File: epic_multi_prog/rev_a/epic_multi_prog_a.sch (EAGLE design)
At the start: 25 parts, among them J1 EPIC-PROG-PORT, J2 MICRO_USB_B_HIROSE_ZX62R-B-5P, J3 MEC1-105-02-XX-XX-D-A, J4 TAG_CONNECT_HEADER_EPIC, U1 FT232RL, U2 MAX1555

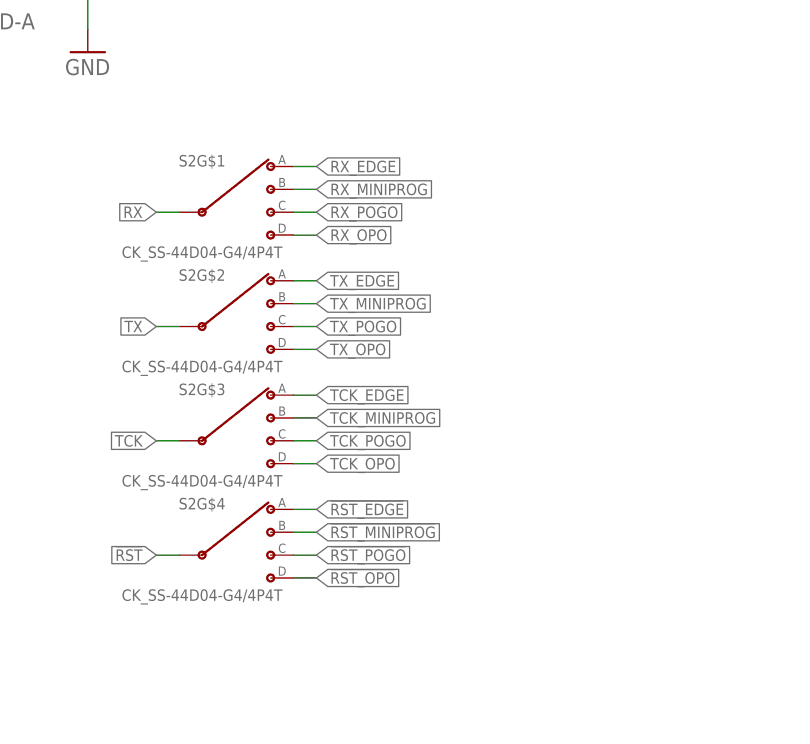
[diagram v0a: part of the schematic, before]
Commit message: Test routing to see how this board is going to look
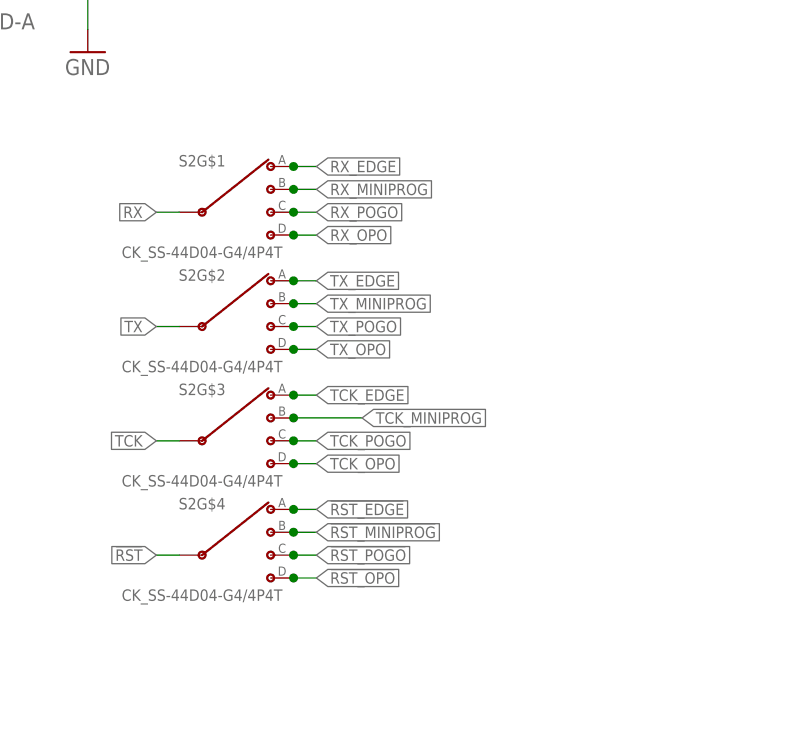
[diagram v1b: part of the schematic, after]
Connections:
- new net !RST_OPO: S2G$4.D
- new net RX_OPO: S2G$1.D
- new net TCK_OPO: S2G$3.D
- new net TX_OPO: S2G$2.D
- net !RST_EDGE: now also S2G$4.A
- net !RST_MINIPROG: now also S2G$4.B
- net !RST_POGO: now also S2G$4.C
- net TCK_EDGE: now also S2G$3.A
- net TCK_MINIPROG: now also S2G$3.B
- net TCK_POGO: now also S2G$3.C
- net TX_EDGE: now also S2G$2.A
- net TX_MINIPROG: now also S2G$2.B
- net TX_POGO: now also S2G$2.C
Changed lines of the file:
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@@
 <wire x1="190.5" y1="96.52" x2="193.04" y2="96.52" width="0.1524" layer="91"/>
 <label x="193.04" y="96.52" size="1.27" layer="95" xref="yes"/>
+<pinref part="S2" gate="G$2" pin="A"/>
+<junction x="190.5" y="96.52"/>
 </segment>
 <segment>
@@
 <wire x1="190.5" y1="93.98" x2="193.04" y2="93.98" width="0.1524" layer="91"/>
 <label x="193.04" y="93.98" size="1.27" layer="95" xref="yes"/>
+<pinref part="S2" gate="G$2" pin="B"/>
+<junction x="190.5" y="93.98"/>
 </segment>
 </net>
@@
 <wire x1="190.5" y1="91.44" x2="193.04" y2="91.44" width="0.1524" layer="91"/>
 <label x="193.04" y="91.44" size="1.27" layer="95" xref="yes"/>
+<pinref part="S2" gate="G$2" pin="C"/>
+<junction x="190.5" y="91.44"/>
 </segment>
 <segment>
@@
 <wire x1="190.5" y1="88.9" x2="193.04" y2="88.9" width="0.1524" layer="91"/>
 <label x="193.04" y="88.9" size="1.27" layer="95" xref="yes"/>
+<pinref part="S2" gate="G$2" pin="D"/>
+<junction x="190.5" y="88.9"/>
 </segment>
 </net>
@@
 <wire x1="190.5" y1="101.6" x2="193.04" y2="101.6" width="0.1524" layer="91"/>
 <label x="193.04" y="101.6" size="1.27" layer="95" xref="yes"/>
+<pinref part="S2" gate="G$1" pin="D"/>
+<junction x="190.5" y="101.6"/>
 </segment>
 </net>
@@
 <wire x1="190.5" y1="104.14" x2="193.04" y2="104.14" width="0.1524" layer="91"/>
 <label x="193.04" y="104.14" size="1.27" layer="95" xref="yes"/>
+<junction x="190.5" y="104.14"/>
 </segment>
 <segment>
@@
 <wire x1="193.04" y1="106.68" x2="190.5" y2="106.68" width="0.1524" layer="91"/>
 <label x="193.04" y="106.68" size="1.27" layer="95" xref="yes"/>
+<junction x="190.5" y="106.68"/>
 </segment>
 </net>
@@
 <wire x1="190.5" y1="109.22" x2="193.04" y2="109.22" width="0.1524" layer="91"/>
 <label x="193.04" y="109.22" size="1.27" layer="95" xref="yes"/>
+<junction x="190.5" y="109.22"/>
 </segment>
 <segment>
@@
 <wire x1="190.5" y1="63.5" x2="193.04" y2="63.5" width="0.1524" layer="91"/>
 <label x="193.04" y="63.5" size="1.27" layer="95" xref="yes"/>
+<pinref part="S2" gate="G$4" pin="D"/>
+<junction x="190.5" y="63.5"/>
 </segment>
 </net>
 <net name="TCK_EDGE" class="0">
-<segment>
-<wire x1="190.5" y1="83.82" x2="193.04" y2="83.82" width="0.1524" layer="91"/>
-<label x="193.04" y="83.82" size="1.27" layer="95" xref="yes"/>
-</segment>
 <segment>
 <pinref part="J3" gate="G$1" pin="9"/>
@@
 <label x="127" y="129.54" size="1.27" layer="95" rot="R180" xref="yes"/>
 </segment>
+<segment>
+<pinref part="S2" gate="G$3" pin="A"/>
+<wire x1="190.5" y1="83.82" x2="193.04" y2="83.82" width="0.1524" layer="91"/>
+<label x="193.04" y="83.82" size="1.27" layer="95" xref="yes"/>
+<junction x="190.5" y="83.82"/>
+</segment>
 </net>
 <net name="TCK_MINIPROG" class="0">
 <segment>
-<wire x1="190.5" y1="81.28" x2="193.04" y2="81.28" width="0.1524" layer="91"/>
-<label x="193.04" y="81.28" size="1.27" layer="95" xref="yes"/>
+<wire x1="190.5" y1="81.28" x2="198.12" y2="81.28" width="0.1524" layer="91"/>
+<label x="198.12" y="81.28" size="1.27" layer="95" xref="yes"/>
+<pinref part="S2" gate="G$3" pin="B"/>
+<junction x="190.5" y="81.28"/>
 </segment>
 <segment>
@@
 <wire x1="190.5" y1="78.74" x2="193.04" y2="78.74" width="0.1524" layer="91"/>
 <label x="193.04" y="78.74" size="1.27" layer="95" xref="yes"/>
+<pinref part="S2" gate="G$3" pin="C"/>
+<junction x="190.5" y="78.74"/>
 </segment>
 <segment>
@@
 <wire x1="190.5" y1="76.2" x2="193.04" y2="76.2" width="0.1524" layer="91"/>
 <label x="193.04" y="76.2" size="1.27" layer="95" xref="yes"/>
+<pinref part="S2" gate="G$3" pin="D"/>
+<junction x="190.5" y="76.2"/>
 </segment>
 </net>
@@
 <wire x1="190.5" y1="71.12" x2="193.04" y2="71.12" width="0.1524" layer="91"/>
 <label x="193.04" y="71.12" size="1.27" layer="95" xref="yes"/>
+<pinref part="S2" gate="G$4" pin="A"/>
+<junction x="190.5" y="71.12"/>
 </segment>
 <segment>
@@
 <wire x1="190.5" y1="68.58" x2="193.04" y2="68.58" width="0.1524" layer="91"/>
 <label x="193.04" y="68.58" size="1.27" layer="95" xref="yes"/>
+<pinref part="S2" gate="G$4" pin="B"/>
+<junction x="190.5" y="68.58"/>
 </segment>
 <segment>
@@
 <wire x1="190.5" y1="66.04" x2="193.04" y2="66.04" width="0.1524" layer="91"/>
 <label x="193.04" y="66.04" size="1.27" layer="95" xref="yes"/>
-</segment>
-<segment>
+<pinref part="S2" gate="G$4" pin="C"/>
+<junction x="190.5" y="66.04"/>
+</segment>
+<segment>

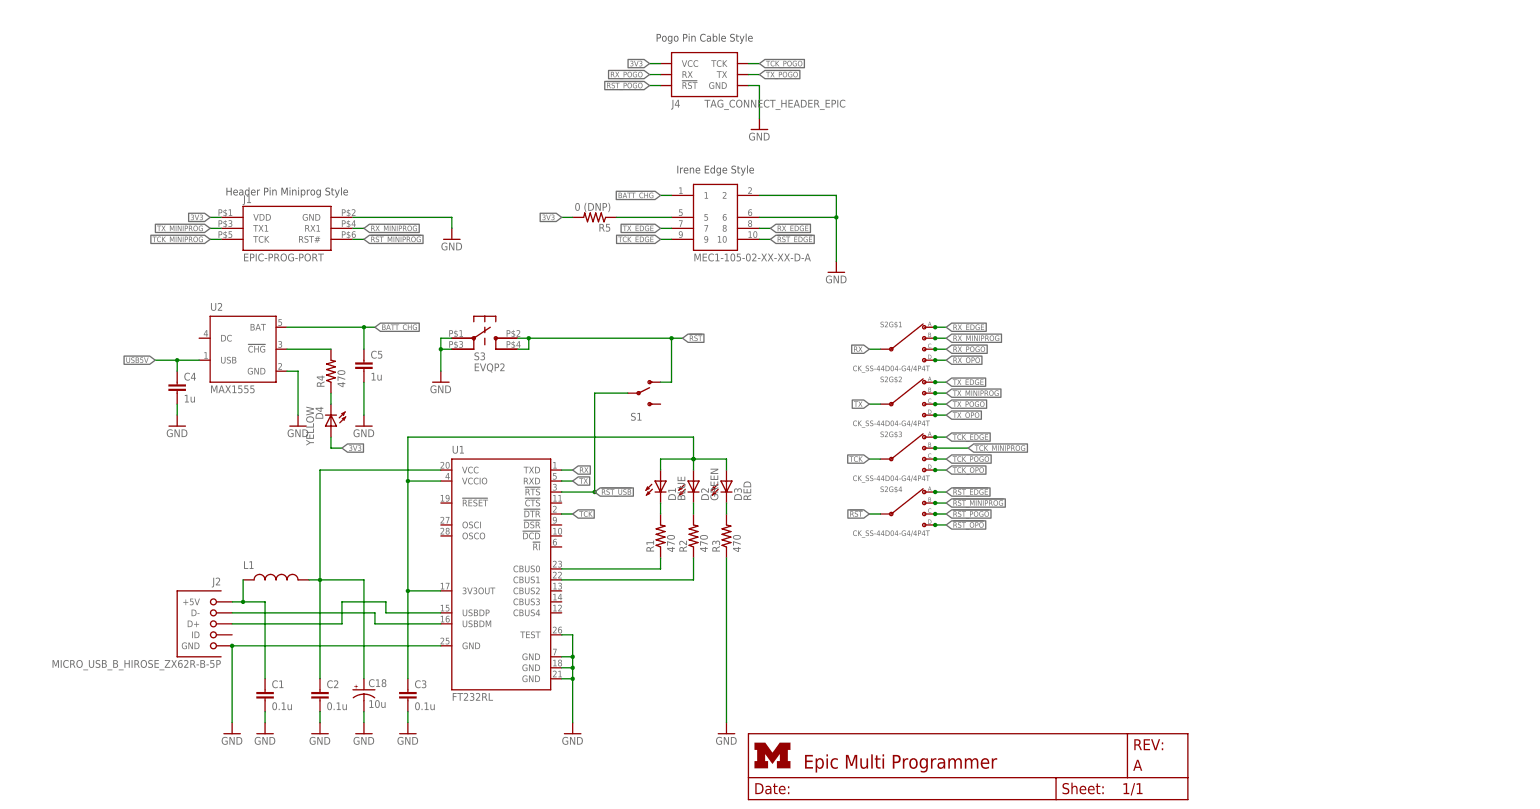
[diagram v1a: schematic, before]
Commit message: added power switches, moving things around
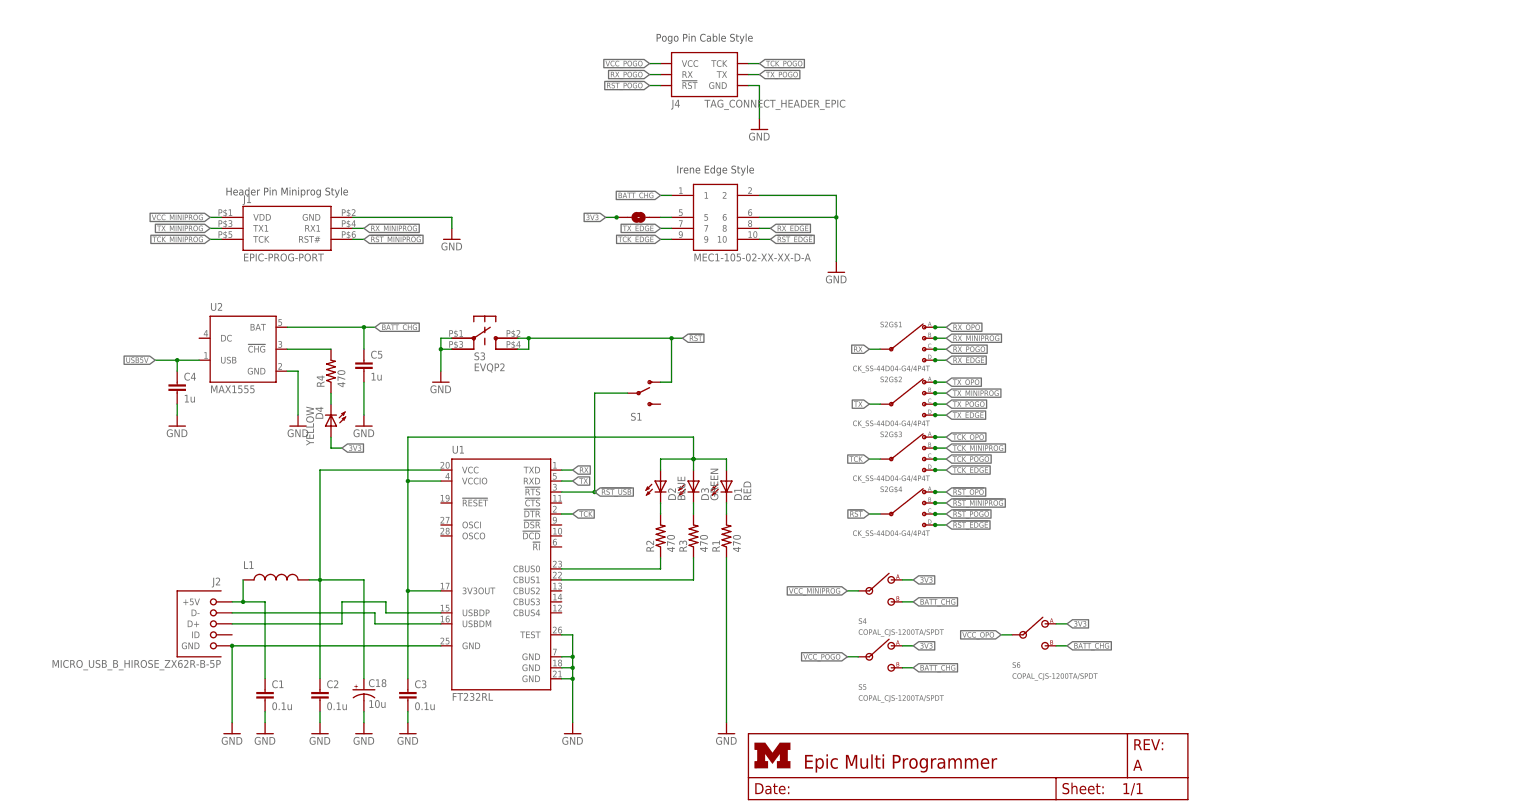
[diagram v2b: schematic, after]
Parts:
- removed R5: 0 (DNP), rcl:R-US_R0603
- added S4, S5, S6: COPAL_CJS-1200TA/SPDT, switches:COPAL_CJS-1200TA/SPDT
- added SJ1: SOLDERJUMPERNO, SparkFun-Passives:SOLDERJUMPERNO
- D1: value BLUE -> RED
- D2: value GREEN -> BLUE
- D3: value RED -> GREEN
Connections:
- new net VCC_MINIPROG: J1.VDD, S4.IN
- new net VCC_OPO: S6.IN
- new net VCC_POGO: J4.VCC, S5.IN
- net !RST_EDGE: now also S2G$4.D; no longer S2G$4.A
- net !RST_OPO: now also S2G$4.A; no longer S2G$4.D
- net 3V3: now also S4.A, S5.A, S6.A, SJ1.1; no longer J1.VDD, J4.VCC, R5.2
- net BATT_CHG: now also S4.B, S5.B, S6.B
- net GND: now also R1.1; no longer R3.1
- net N$1: now also SJ1.2; no longer R5.1
- net N$10: now also R2.1; no longer R1.1
- net N$11: now also R3.1; no longer R2.1
- net RX_EDGE: now also S2G$1.D; no longer S2G$1.A
- net RX_OPO: now also S2G$1.A; no longer S2G$1.D
- net TCK_EDGE: now also S2G$3.D; no longer S2G$3.A
- net TCK_OPO: now also S2G$3.A; no longer S2G$3.D
- net TX_EDGE: now also S2G$2.D; no longer S2G$2.A
- net TX_OPO: now also S2G$2.A; no longer S2G$2.D
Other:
- moved on the sheet: D1, D2, D3, R1, R2, R3

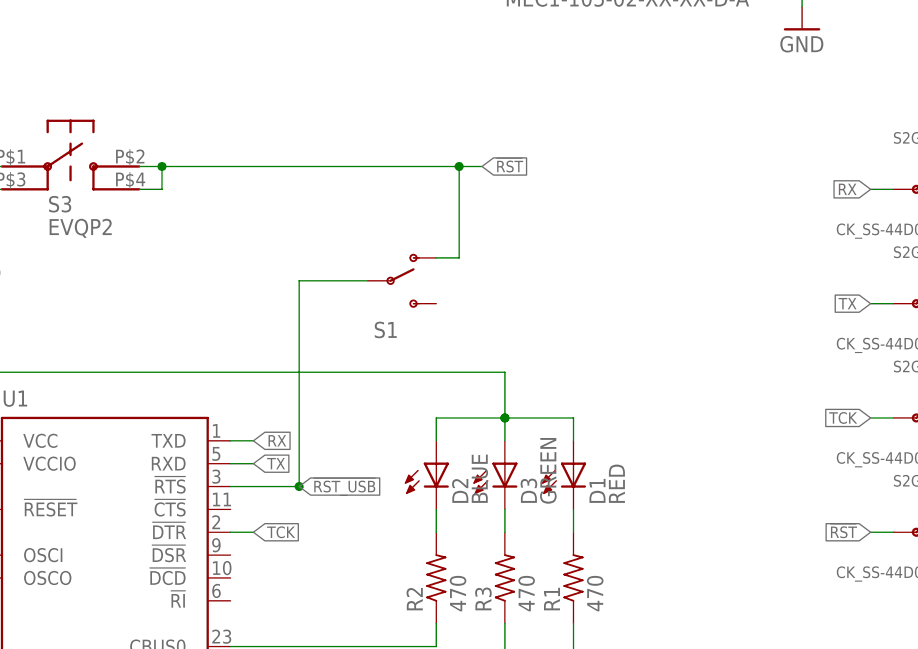
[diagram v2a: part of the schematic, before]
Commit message: Moved uart/prog switch
Planning on the huge smd micro usb
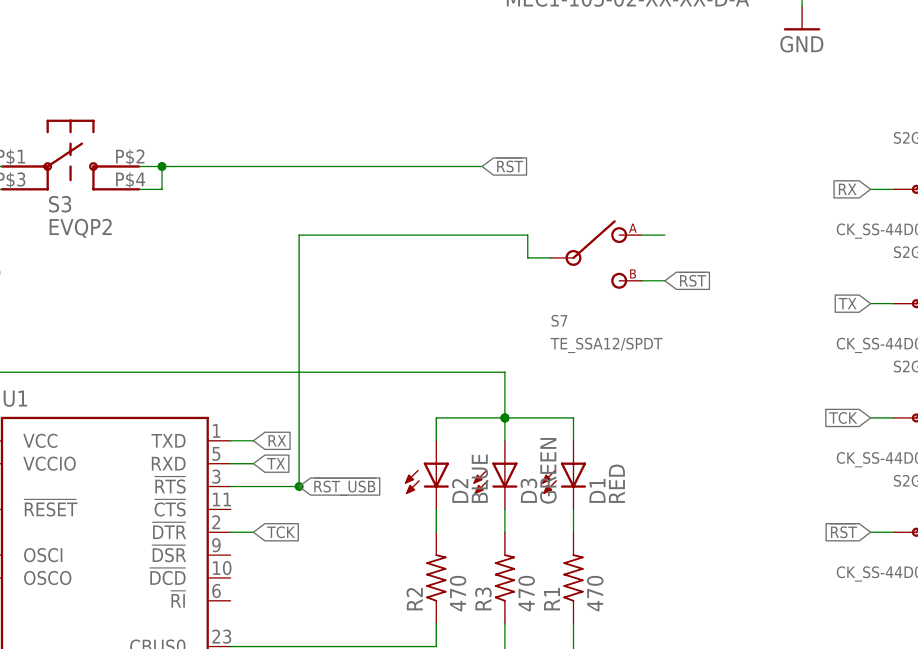
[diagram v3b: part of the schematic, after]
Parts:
- removed S1: (no value), SparkFun:SWITCH-SPSTPTH
- added S7: TE_SSA12/SPDT, switches:TE_SSA12/SPDT
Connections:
- new net N$13: S7.A
- net !RST: now also S7.B; no longer S1.O
- net !RST_USB: now also S7.IN; no longer S1.P
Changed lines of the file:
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@@
 </part>
 <part name="GND8" library="supply1" deviceset="GND" device=""/>
-<part name="S1" library="SparkFun" deviceset="SWITCH-SPST" device="PTH">
-<attribute name="DIGIKEY" value="EG1903-ND"/>
-</part>
 <part name="FRAME5" library="nest_interface" deviceset="LETTER_L" device=""/>
 <part name="J2" library="connector" deviceset="MICRO_USB_B_HIROSE_ZX62R-B-5P" device=""/>
@@
 <part name="S5" library="switches" deviceset="COPAL_CJS-1200TA/SPDT" device=""/>
 <part name="S6" library="switches" deviceset="COPAL_CJS-1200TA/SPDT" device=""/>
+<part name="S7" library="switches" deviceset="TE_SSA12/SPDT" device=""/>
 </parts>
 <sheets>
@@
 </instance>
 <instance part="GND8" gate="1" x="76.2" y="96.52"/>
-<instance part="S1" gate="1" x="121.92" y="93.98">
-<attribute name="DIGIKEY" x="121.92" y="93.98" size="1.778" layer="96" display="off"/>
-</instance>
 <instance part="FRAME5" gate="G$1" x="0" y="0"/>
 <instance part="FRAME5" gate="G$2" x="147.32" y="0"/>
@@
 <instance part="S5" gate="G$1" x="175.26" y="33.02"/>
 <instance part="S6" gate="G$1" x="210.82" y="38.1"/>
+<instance part="S7" gate="G$1" x="142.24" y="96.52"/>
 </instances>
 <busses>
@@
 <wire x1="96.52" y1="106.68" x2="93.98" y2="106.68" width="0.1524" layer="91"/>
 <junction x="96.52" y="106.68"/>
-<wire x1="96.52" y1="106.68" x2="129.54" y2="106.68" width="0.1524" layer="91"/>
-<pinref part="S1" gate="1" pin="O"/>
-<wire x1="127" y1="96.52" x2="129.54" y2="96.52" width="0.1524" layer="91"/>
-<wire x1="129.54" y1="96.52" x2="129.54" y2="106.68" width="0.1524" layer="91"/>
-<wire x1="129.54" y1="106.68" x2="132.08" y2="106.68" width="0.1524" layer="91"/>
-<junction x="129.54" y="106.68"/>
+<wire x1="96.52" y1="106.68" x2="132.08" y2="106.68" width="0.1524" layer="91"/>
 <label x="132.08" y="106.68" size="1.27" layer="95" xref="yes"/>
 </segment>
@@
 <label x="175.26" y="66.04" size="1.27" layer="95" rot="R180" xref="yes"/>
 </segment>
+<segment>
+<pinref part="S7" gate="G$1" pin="B"/>
+<wire x1="149.86" y1="93.98" x2="152.4" y2="93.98" width="0.1524" layer="91"/>
+<label x="152.4" y="93.98" size="1.27" layer="95" xref="yes"/>
+</segment>
 </net>
 <net name="!RST_USB" class="0">
@@
 <pinref part="U1" gate="1" pin="!RTS"/>
 <wire x1="104.14" y1="71.12" x2="111.76" y2="71.12" width="0.1524" layer="91"/>
-<wire x1="111.76" y1="71.12" x2="111.76" y2="93.98" width="0.1524" layer="91"/>
-<pinref part="S1" gate="1" pin="P"/>
-<wire x1="111.76" y1="93.98" x2="119.38" y2="93.98" width="0.1524" layer="91"/>
+<wire x1="111.76" y1="71.12" x2="111.76" y2="99.06" width="0.1524" layer="91"/>
 <junction x="111.76" y="71.12"/>
 <label x="111.76" y="71.12" size="1.27" layer="95" xref="yes"/>
+<wire x1="111.76" y1="99.06" x2="137.16" y2="99.06" width="0.1524" layer="91"/>
+<wire x1="137.16" y1="99.06" x2="137.16" y2="96.52" width="0.1524" layer="91"/>
+<pinref part="S7" gate="G$1" pin="IN"/>
+<wire x1="137.16" y1="96.52" x2="139.7" y2="96.52" width="0.1524" layer="91"/>
 </segment>
 </net>
@@
 </segment>
 </net>
+<net name="N$13" class="0">
+<segment>
+<pinref part="S7" gate="G$1" pin="A"/>
+<wire x1="149.86" y1="99.06" x2="152.4" y2="99.06" width="0.1524" layer="91"/>
+</segment>
+</net>

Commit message: Nearly routed, added more max1555s
Decided that each circuit should have its own charging led.
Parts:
- added C10, C11, C6, C7, C8, C9: 1u, rcl:C-EUC0603
- added D5, D6, D7: YELLOW, SparkFun:LED0603
- added J5: MICRO_USB_B_MALE_HIROSE_ZX80-B-5S, connector:MICRO_USB_B_MALE_HIROSE_ZX80-B-5S
- added R5, R6, R7: 470, rcl:R-US_R0603
- added U3, U4, U5: MAX1555, maxim:MAX1555
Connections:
- removed net BATT_CHG: C5.1, J3.1, S4.B, S5.B, S6.B, U2.BAT
- new net BATT_CHG_EDGE: C9.1, J3.1, U4.BAT
- new net BATT_CHG_MINIPROG: C7.1, S4.B, U3.BAT
- new net BATT_CHG_OPO: C5.1, S6.B, U2.BAT
- new net BATT_CHG_POGO: C11.1, S5.B, U5.BAT
- new net N$14: J5.D+
- new net N$15: J5.ID
- new net N$16: R5.2, U3.!CHG
- new net N$17: J5.SHIELD
- new net N$18: D6.C, R6.1
- new net N$19: R6.2, U4.!CHG
- new net N$20: D7.C, R7.1
- new net N$21: R7.2, U5.!CHG
- new net N$5: D5.C, R5.1
- net !RST: now also S7.A; no longer S7.B
- net 3V3: now also D5.A, D6.A, D7.A
- net GND: now also C10.2, C11.2, C6.2, C7.2, C8.2, C9.2, J5.GND, U3.GND, U4.GND, U5.GND
- net N$13: now also J5.D-; no longer S7.A
- net USB5V: now also C10.1, C6.1, C8.1, U3.USB, U4.USB, U5.USB
- net VCC_OPO: now also J5.+5V
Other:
- moved on the sheet: C4

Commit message: added bom
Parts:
- C1, C2, C3: DIGIKEY (none) -> 445-1316-1-ND
- C10, C11, C4, C5, C6, C7, C8, C9: DIGIKEY (none) -> 445-1321-1-ND
- J3: DIGIKEY (none) -> SAM8115-ND
- J5: MOUSER (none) -> 798-ZX80-B-5S
- S2: DIGIKEY (none) -> CKN10389-ND
- U2, U3, U4, U5: DIGIKEY (none) -> MAX1555EZK+TCT-ND
